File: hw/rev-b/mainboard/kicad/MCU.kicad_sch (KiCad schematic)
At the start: 34 parts, among them J23 MENU_HDR, SW4 RUN, SW5 MENU_BTN, U21 RP2040, Y1 12 MHz

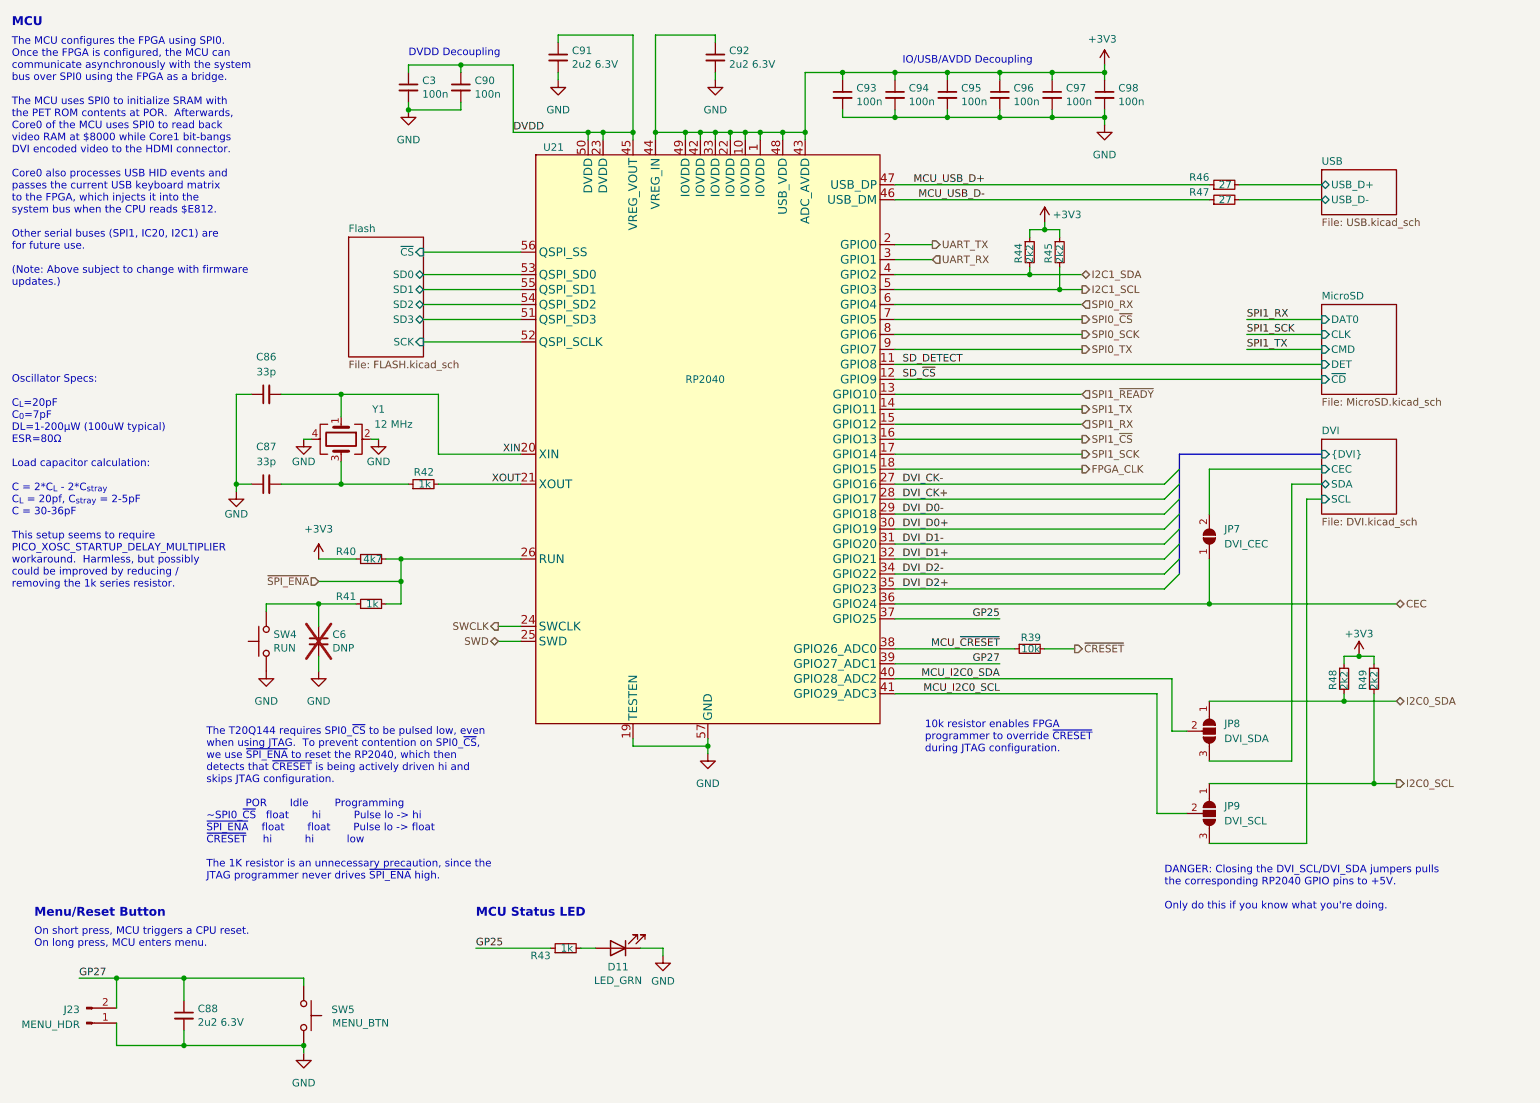
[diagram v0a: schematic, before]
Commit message: fix(hw): add 100n on RUN pin to improve EMI immunity
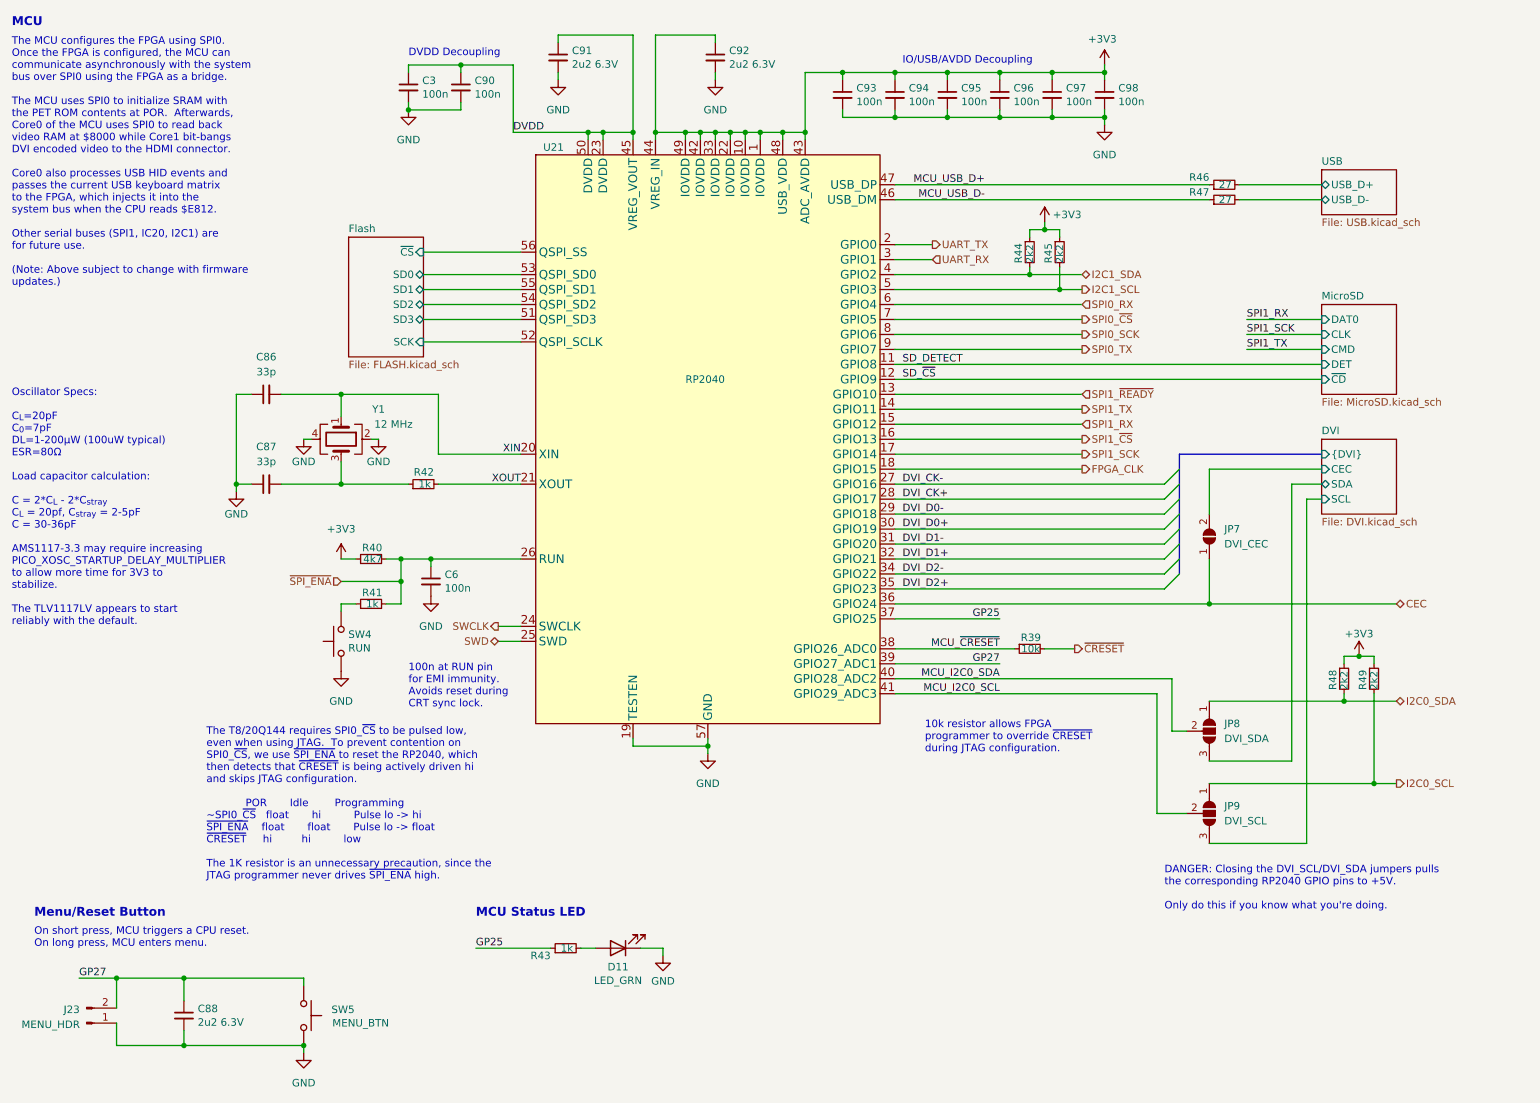
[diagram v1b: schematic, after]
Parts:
- C6: value DNP -> 100n; LCSC (none) -> C307331; now fitted
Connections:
- net ~{SPI_ENA}: now also C6.1
- net at R41.1, SW4.2: no longer C6.1
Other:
- note added: "100n at RUN pin for EMI immunity. Avoids reset during CRT sync lock."
- note added: "10k resistor allows FPGA programmer to override ~{CRESET} during JTAG configuration."
- note added: "Oscillator Specs: C_{L}=20pF C_{0}=7pF DL=1-200μW (100uW typical) ESR=80Ω Load capacitor calculation: C = 2*C_{L} - 2*C_{stray} C_{L} = 20pf, C_{stray} = 2-5pF C = 30-36pF AMS1117-3.3 may require increasing PICO_XOSC_STARTUP_DELAY_MULTIPLIER to allow more time for 3V3 to stabilize. The TLV1117LV appears to start reliably with the default."
- note added: "The T8/20Q144 requires SPI0_~{CS} to be pulsed low, even when using JTAG. To prevent contention on SPI0_~{CS}, we use ~{SPI_ENA} to reset the RP2040, which then detects that ~{CRESET} is being actively driven hi and skips JTAG configuration. POR Idle Programming ~SPI0_~{CS} float hi Pulse lo -> hi ~{SPI_ENA} float float Pulse lo -> float ~{CRESET} hi hi low The 1K resistor is an unnecessary preca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"
- note removed: "10k resistor enables FPGA programmer to override ~{CRESET} during JTAG configuration."
- note removed: "Oscillator Specs: C_{L}=20pF C_{0}=7pF DL=1-200μW (100uW typical) ESR=80Ω Load capacitor calculation: C = 2*C_{L} - 2*C_{stray} C_{L} = 20pf, C_{stray} = 2-5pF C = 30-36pF This setup seems to require PICO_XOSC_STARTUP_DELAY_MULTIPLIER workaround. Harmless, but possibly could be improved by reducing / removing the 1k series resistor."
- note removed: "The T20Q144 requires SPI0_~{CS} to be pulsed low, even when using JTAG. To prevent contention on SPI0_~{CS}, we use ~{SPI_ENA} to reset the RP2040, which then detects that ~{CRESET} is being actively driven hi and skips JTAG configuration. POR Idle Programming ~SPI0_~{CS} float hi Pulse lo -> hi ~{SPI_ENA} float float Pulse lo -> float ~{CRESET} hi hi low The 1K resistor is an unnecessary precaut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"
- moved on the sheet: SW4

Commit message: cr(hw): use SMD push buttons
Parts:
- SW4: footprint EconoPET:SW_PUSH_1P1T_6x3.5mm_H4.3_APEM_MJTP1243 -> LCSC:SW-SMD_L3.9-W3.0-P4.45; LCSC (none) -> C720477
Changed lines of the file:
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@@
 			)
 		)
-		(property "Footprint" "EconoPET:SW_PUSH_1P1T_6x3.5mm_H4.3_APEM_MJTP1243"
+		(property "Footprint" "LCSC:SW-SMD_L3.9-W3.0-P4.45"
 			(at 66.04 121.92 0)
 			(effects
@@
 			)
 		)
-		(property "Datasheet" "~"
+		(property "Datasheet" "https://jlcpcb.com/api/file/downloadByFileSystemAccessId/8588886944068096000"
 			(at 66.04 121.92 0)
 			(effects
@@
 			)
 		)
-		(property "LCSC" ""
+		(property "LCSC" "C720477"
 			(at 71.12 121.92 90)
 			(effects
